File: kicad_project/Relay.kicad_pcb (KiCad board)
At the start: 2 copper layers, 39.6 x 28.3 mm, 13 parts, among them J1 5018762640, J2 USB_C_Receptacle, J3 RJ45, K1 G6K-2P-Y_DC3, Q1 SO2222

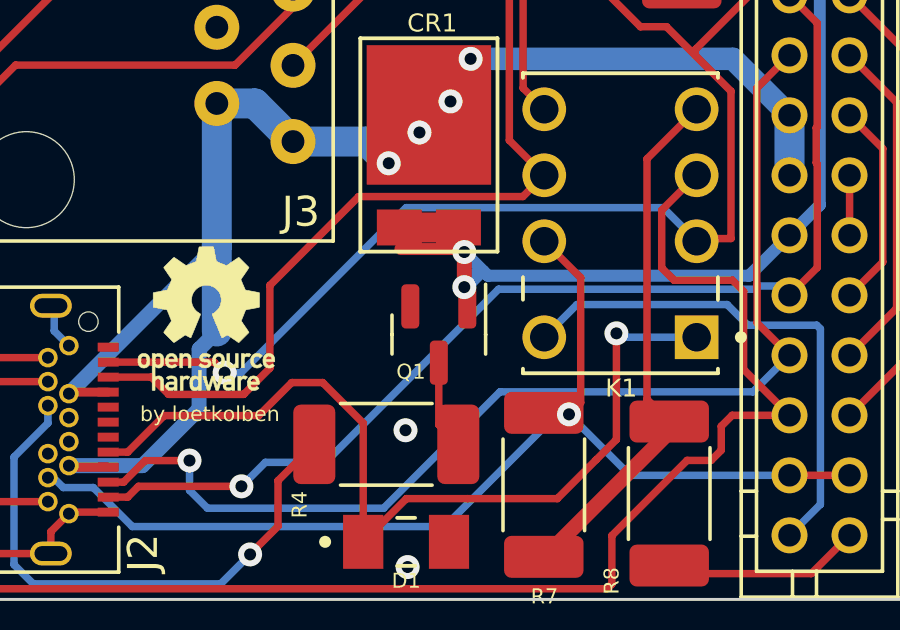
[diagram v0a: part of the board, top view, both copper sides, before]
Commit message: symbol SO2222 updated Symbol
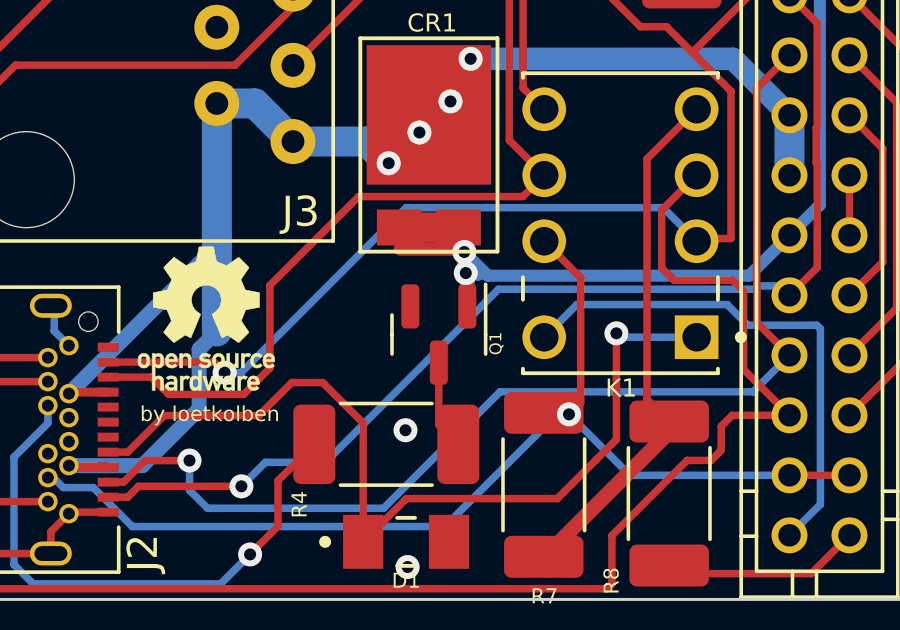
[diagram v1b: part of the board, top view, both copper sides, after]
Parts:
- K1: value G6K-2P-Y_DC3 -> G6K-2P-Y_DC5

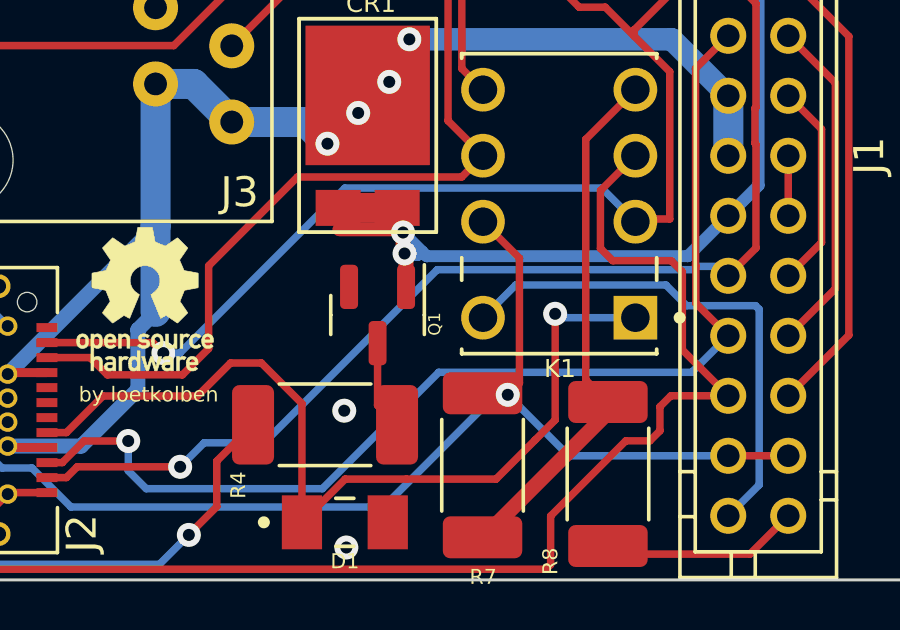
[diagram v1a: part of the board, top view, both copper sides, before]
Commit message: new NPN Transistor
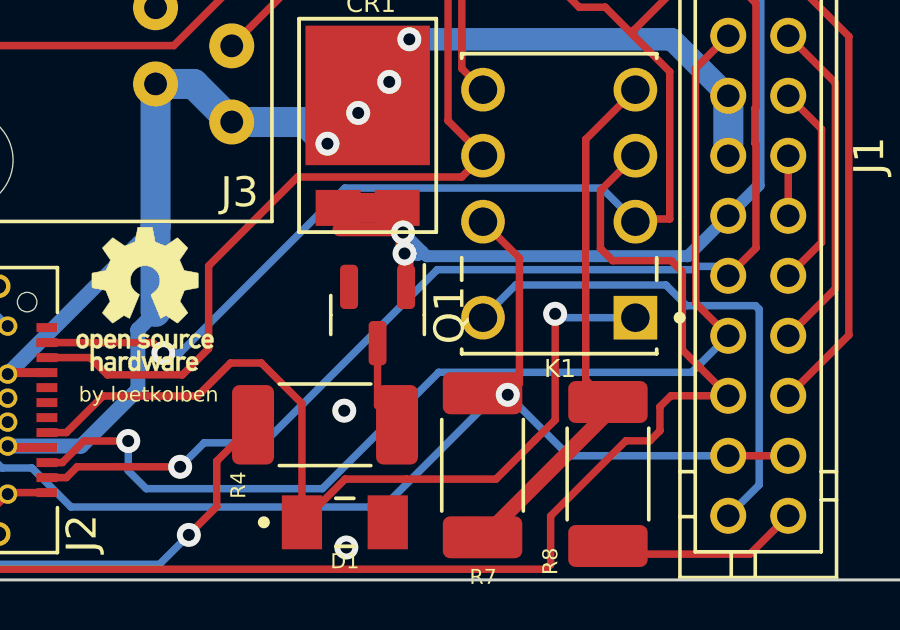
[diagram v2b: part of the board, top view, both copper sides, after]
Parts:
- Q1: value SO2222 -> CMPT5551
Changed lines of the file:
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@@
   (net 28 "CAN2_H")
   (net 29 "Relay_5")
-  (net 30 "Net-(R4-Pad1)")
+  (net 30 "Net-(Q1-Pad3)")
+  (footprint "Package_TO_SOT_SMD:SOT-23" (layer "F.Cu")
+    (at 162.46 71.9 -90)
+    (descr "SOT, 3 Pin (https://www.jedec.org/system/files/docs/to-236h.pdf variant AB), generated with kicad-footprint-generator ipc_gullwing_generator.py")
+    (tags "SOT TO_SOT_SMD")
+    (property "Sheetfile" "Relay.kicad_sch")
+    (property "Sheetname" "")
+    (attr smd)
+    (fp_text reference "Q1" (at 0 -2.4 90) (layer "F.SilkS")
+      (effects (font (size 1 1) (thickness 0.15)))
+    )
+    (fp_text value "CMPT5551" (at 0 2.4 90) (layer "F.Fab")
+      (effects (font (size 1 1) (thickness 0.15)))
+    )
+    (fp_text user "${REFERENCE}" (at 0 0 90) (layer "F.Fab")
+      (effects (font (size 0.32 0.32) (thickness 0.05)))
+    )
+    (fp_line (start 0 1.56) (end -0.65 1.56) (layer "F.SilkS") (width 0.12))
+    (fp_line (start 0 -1.56) (end -1.675 -1.56) (layer "F.SilkS") (width 0.12))
+    (fp_line (start 0 -1.56) (end 0.65 -1.56) (layer "F.SilkS") (width 0.12))
+    (fp_line (start 0 1.56) (end 0.65 1.56) (layer "F.SilkS") (width 0.12))
+    (fp_line (start 1.92 -1.7) (end -1.92 -1.7) (layer "F.CrtYd") (width 0.05))
+    (fp_line (start -1.92 -1.7) (end -1.92 1.7) (layer "F.CrtYd") (width 0.05))
+    (fp_line (start -1.92 1.7) (end 1.92 1.7) (layer "F.CrtYd") (width 0.05))
+    (fp_line (start 1.92 1.7) (end 1.92 -1.7) (layer "F.CrtYd") (width 0.05))
+    (fp_line (start -0.65 -1.125) (end -0.325 -1.45) (layer "F.Fab") (width 0.1))
+    (fp_line (start 0.65 -1.45) (end 0.65 1.45) (layer "F.Fab") (width 0.1))
+    (fp_line (start 0.65 1.45) (end -0.65 1.45) (layer "F.Fab") (width 0.1))
+    (fp_line (start -0.325 -1.45) (end 0.65 -1.45) (layer "F.Fab") (width 0.1))
+    (fp_line (start -0.65 1.45) (end -0.65 -1.125) (layer "F.Fab") (width 0.1))
+    (pad "1" smd roundrect (at -0.9375 -0.95 270) (size 1.475 0.6) (layers "F.Cu" "F.Paste" "F.Mask") (roundrect_rratio 0.25)
+      (net 3 "IGN") (pinfunction "B") (pintype "input"))
+    (pad "2" smd roundrect (at -0.9375 0.95 270) (size 1.475 0.6) (layers "F.Cu" "F.Paste" "F.Mask") (roundrect_rratio 0.25)
+      (net 2 "GND") (pinfunction "E") (pintype "passive"))
+    (pad "3" smd roundrect (at 0.9375 0 270) (size 1.475 0.6) (layers "F.Cu" "F.Paste" "F.Mask") (roundrect_rratio 0.25)
+      (net 30 "Net-(Q1-Pad3)") (pinfunction "C") (pintype "passive"))
+    (model "${KICAD6_3DMODEL_DIR}/Package_TO_SOT_SMD.3dshapes/SOT-23.wrl"
+      (offset (xyz 0 0 0))
+      (scale (xyz 1 1 1))
+      (rotate (xyz 0 0 0))
+    )
+  )
   (footprint "Relay:DIO_BAV21W_RHG" (layer "F.Cu")
     (at 161.37 78.81)
@@
       (net 27 "Net-(J1-Pad25)") (pintype "passive"))
     (model "${KICAD6_3DMODEL_DIR}/Resistor_SMD.3dshapes/R_2010_5025Metric.wrl"
-      (offset (xyz 0 0 0))
-      (scale (xyz 1 1 1))
-      (rotate (xyz 0 0 0))
-    )
-  )
-  (footprint "Package_TO_SOT_SMD:SOT-23" (layer "F.Cu")
-    (at 162.46 71.9 -90)
-    (descr "SOT, 3 Pin (https://www.jedec.org/system/files/docs/to-236h.pdf variant AB), generated with kicad-footprint-generator ipc_gullwing_generator.py")
-    (tags "SOT TO_SOT_SMD")
-    (property "Sheetfile" "Relay.kicad_sch")
-    (property "Sheetname" "")
-    (attr smd)
-    (fp_text reference "Q1" (at 0.3 -1.9 90) (layer "F.SilkS")
-      (effects (font (size 0.4 0.4) (thickness 0.1)))
-    )
-    (fp_text value "SO2222" (at 0 2.4 90) (layer "F.Fab")
-      (effects (font (size 1 1) (thickness 0.15)))
-    )
-    (fp_text user "${REFERENCE}" (at 0 0 90) (layer "F.Fab")
-      (effects (font (size 0.32 0.32) (thickness 0.05)))
-    )
-    (fp_line (start 0 1.56) (end 0.65 1.56) (layer "F.SilkS") (width 0.12))
-    (fp_line (start 0 1.56) (end -0.65 1.56) (layer "F.SilkS") (width 0.12))
-    (fp_line (start 0 -1.56) (end 0.65 -1.56) (layer "F.SilkS") (width 0.12))
-    (fp_line (start 0 -1.56) (end -1.675 -1.56) (layer "F.SilkS") (width 0.12))
-    (fp_line (start -1.92 1.7) (end 1.92 1.7) (layer "F.CrtYd") (width 0.05))
-    (fp_line (start 1.92 1.7) (end 1.92 -1.7) (layer "F.CrtYd") (width 0.05))
-    (fp_line (start 1.92 -1.7) (end -1.92 -1.7) (layer "F.CrtYd") (width 0.05))
-    (fp_line (start -1.92 -1.7) (end -1.92 1.7) (layer "F.CrtYd") (width 0.05))
-    (fp_line (start -0.325 -1.45) (end 0.65 -1.45) (layer "F.Fab") (width 0.1))
-    (fp_line (start 0.65 1.45) (end -0.65 1.45) (layer "F.Fab") (width 0.1))
-    (fp_line (start -0.65 1.45) (end -0.65 -1.125) (layer "F.Fab") (width 0.1))
-    (fp_line (start 0.65 -1.45) (end 0.65 1.45) (layer "F.Fab") (width 0.1))
-    (fp_line (start -0.65 -1.125) (end -0.325 -1.45) (layer "F.Fab") (width 0.1))
-    (pad "1" smd roundrect (at -0.9375 -0.95 270) (size 1.475 0.6) (layers "F.Cu" "F.Paste" "F.Mask") (roundrect_rratio 0.25)
-      (net 3 "IGN") (pinfunction "B") (pintype "input"))
-    (pad "2" smd roundrect (at -0.9375 0.95 270) (size 1.475 0.6) (layers "F.Cu" "F.Paste" "F.Mask") (roundrect_rratio 0.25)
-      (net 2 "GND") (pinfunction "C") (pintype "passive"))
-    (pad "3" smd roundrect (at 0.9375 0 270) (size 1.475 0.6) (layers "F.Cu" "F.Paste" "F.Mask") (roundrect_rratio 0.25)
-      (net 30 "Net-(R4-Pad1)") (pinfunction "E") (pintype "passive"))
-    (model "${KICAD6_3DMODEL_DIR}/Package_TO_SOT_SMD.3dshapes/SOT-23.wrl"
       (offset (xyz 0 0 0))
       (scale (xyz 1 1 1))
@@
     (fp_line (start 2.5 1.25) (end -2.5 1.25) (layer "F.Fab") (width 0.1))
     (pad "1" smd roundrect (at -2.4 0 180) (size 1.4 2.65) (layers "F.Cu" "F.Paste" "F.Mask") (roundrect_rratio 0.1785707143)
-      (net 30 "Net-(R4-Pad1)") (pintype "passive"))
+      (net 30 "Net-(Q1-Pad3)") (pintype "passive"))
     (pad "2" smd roundrect (at 2.4 0 180) (size 1.4 2.65) (layers "F.Cu" "F.Paste" "F.Mask") (roundrect_rratio 0.1785707143)
       (net 21 "SBU2") (pintype "passive"))

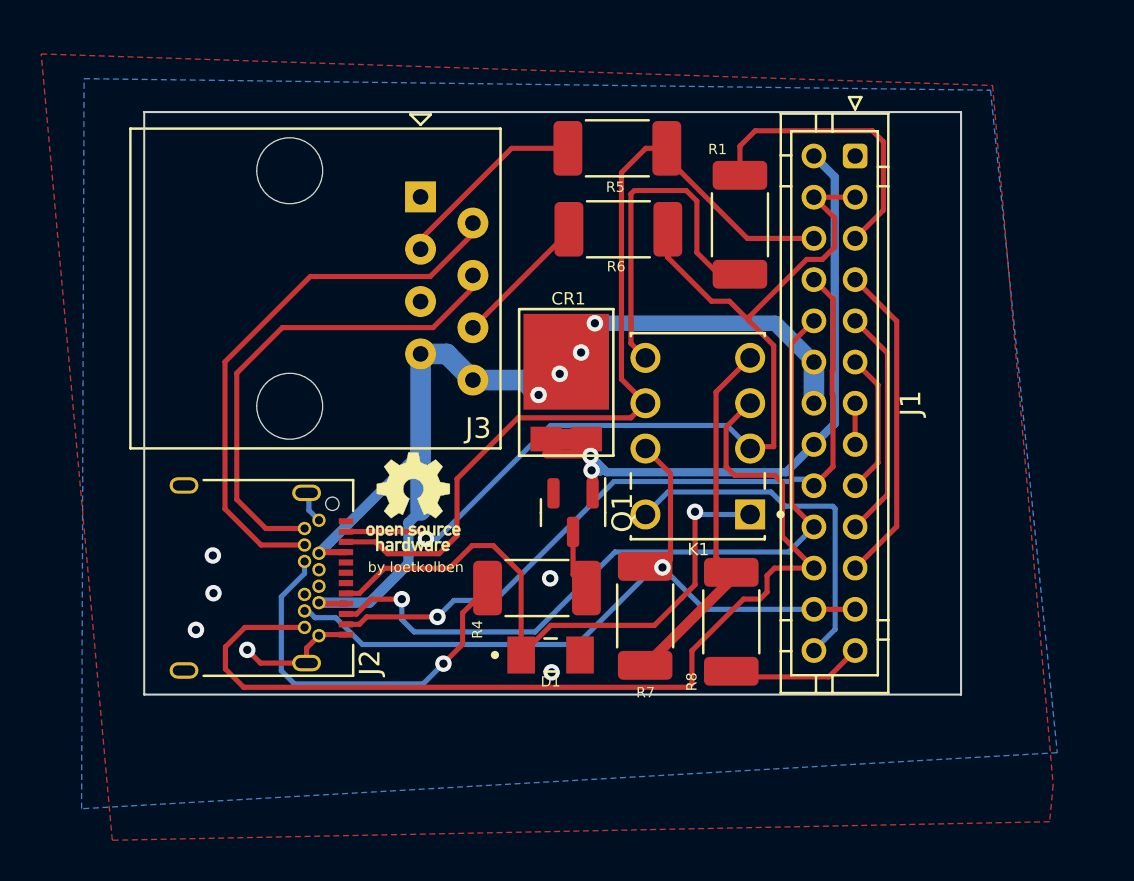
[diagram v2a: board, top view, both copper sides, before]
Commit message: back to SO2222 NPN Transistor
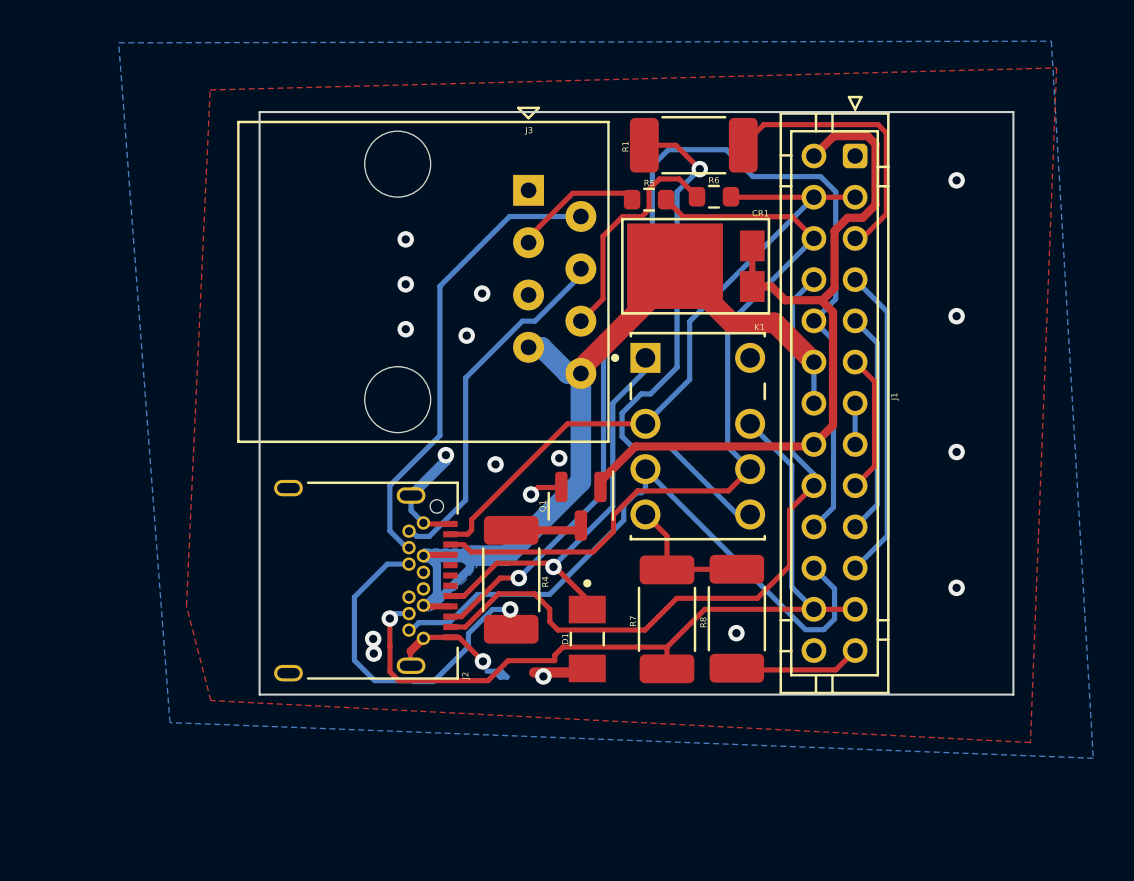
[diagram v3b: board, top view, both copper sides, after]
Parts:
- R5, R6: footprint Resistor_SMD:R_2010_5025Metric_Pad1.40x2.65mm_HandSolder -> Resistor_SMD:R_0603_1608Metric
- moved CR1 8.44 mm to (168.4, 59.9), turned to 0 degrees
- moved J3 5.25 mm to (160.3, 56.3)
- moved J2 5.07 mm to (151.5, 75.2)
- moved R6 4.90 mm to (169.3, 56.6)
- moved R1 4.46 mm to (168.3, 54.1), turned to 180 degrees
- moved R5 2.93 mm to (166.2, 56.7)
- moved D1 1.94 mm to (163.2, 78.0), turned to -90 degrees
- moved R4 1.31 mm to (159.5, 75.2), turned to -90 degrees
- moved R7 1.07 mm to (167.0, 77.1), turned to -90 degrees
- moved Q1 0.49 mm to (162.8, 71.6)
- moved R8 0.31 mm to (170.4, 77.0)
- turned K1 to 0 degrees
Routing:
- net CAN2_H: track 49.4 -> 31.2 mm
- net CAN1_L: track 37.3 -> 54.3 mm
- net CAN0_H: track 47.5 -> 32.4 mm, vias 1 -> 0
- net Relay_4: track 17.8 -> 6.51 mm
- net Relay_5: track 16.8 -> 25.8 mm, vias 0 -> 1
- net SBU1: track 30.1 -> 21.2 mm
- net GND: track 24.9 -> 16.5 mm, vias 6 -> 18
- net CAN3_H: track 23.8 -> 17.5 mm
- net CAN0_L: track 43.0 -> 38.2 mm
- net Net-(J3-Pad6): track 6.71 -> 11.2 mm
- net CAN3_L: track 26.8 -> 22.4 mm
- net +12V: track 49.8 -> 45.3 mm, vias 4 -> 0
- net Net-(J3-Pad3): track 9.46 -> 6.29 mm
- net IGN: track 34.8 -> 37.5 mm, vias 2 -> 0
- net CAN2_L: track 37.1 -> 39.5 mm
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- added copper zone on B.Cu, net +12V
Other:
- board size 39.6 x 28.3 mm -> 36.6 x 28.3 mm
